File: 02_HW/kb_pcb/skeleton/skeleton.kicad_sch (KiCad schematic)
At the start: 60 parts, among them SW1 SW_Push, SW10 SW_Push, SW11 SW_Push, SW12 SW_Push, SW13 SW_Push, SW14 SW_Push, SW15 SW_Push, SW16 SW_Push, SW17 SW_Push, SW18 SW_Push, SW19 SW_Push, SW2 SW_Push, SW20 SW_Push, SW21 SW_Push, SW22 SW_Push, SW23 SW_Push, SW24 SW_Push, SW25 SW_Push, SW26 SW_Push, SW27 SW_Push, SW28 SW_Push, SW29 SW_Push, SW3 SW_Push, SW30 SW_Push, SW4 SW_Push, SW5 SW_Push, SW6 SW_Push, SW7 SW_Push, SW8 SW_Push, SW9 SW_Push

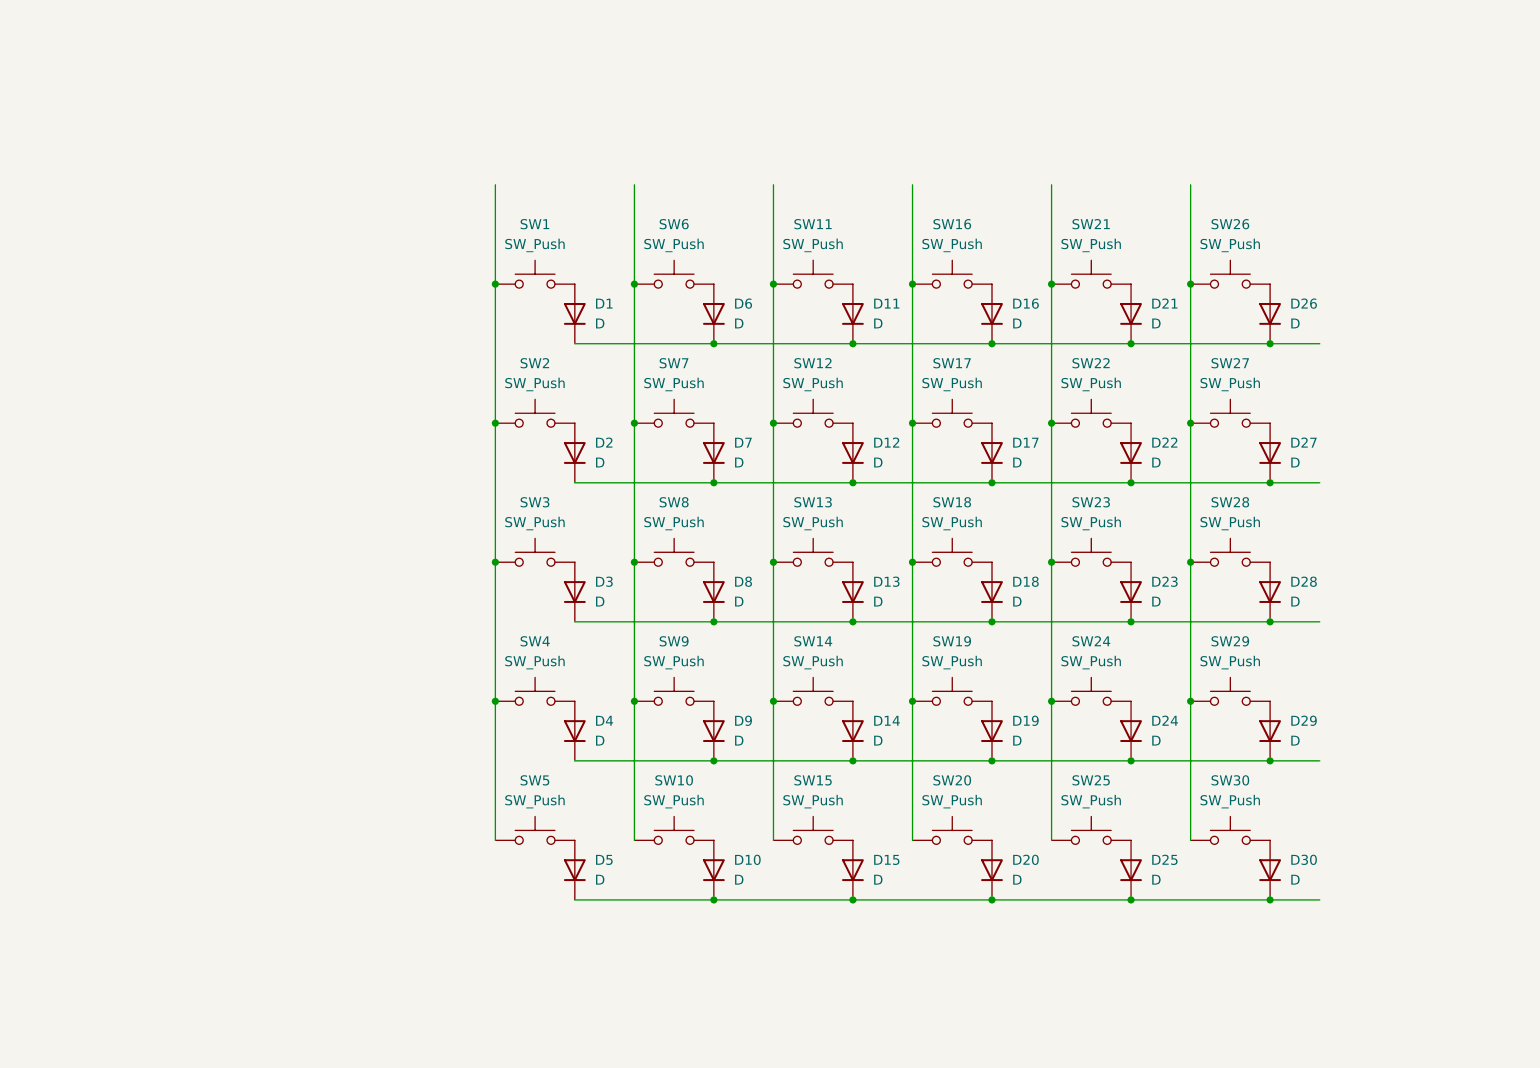
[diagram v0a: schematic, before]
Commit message: Added footprints
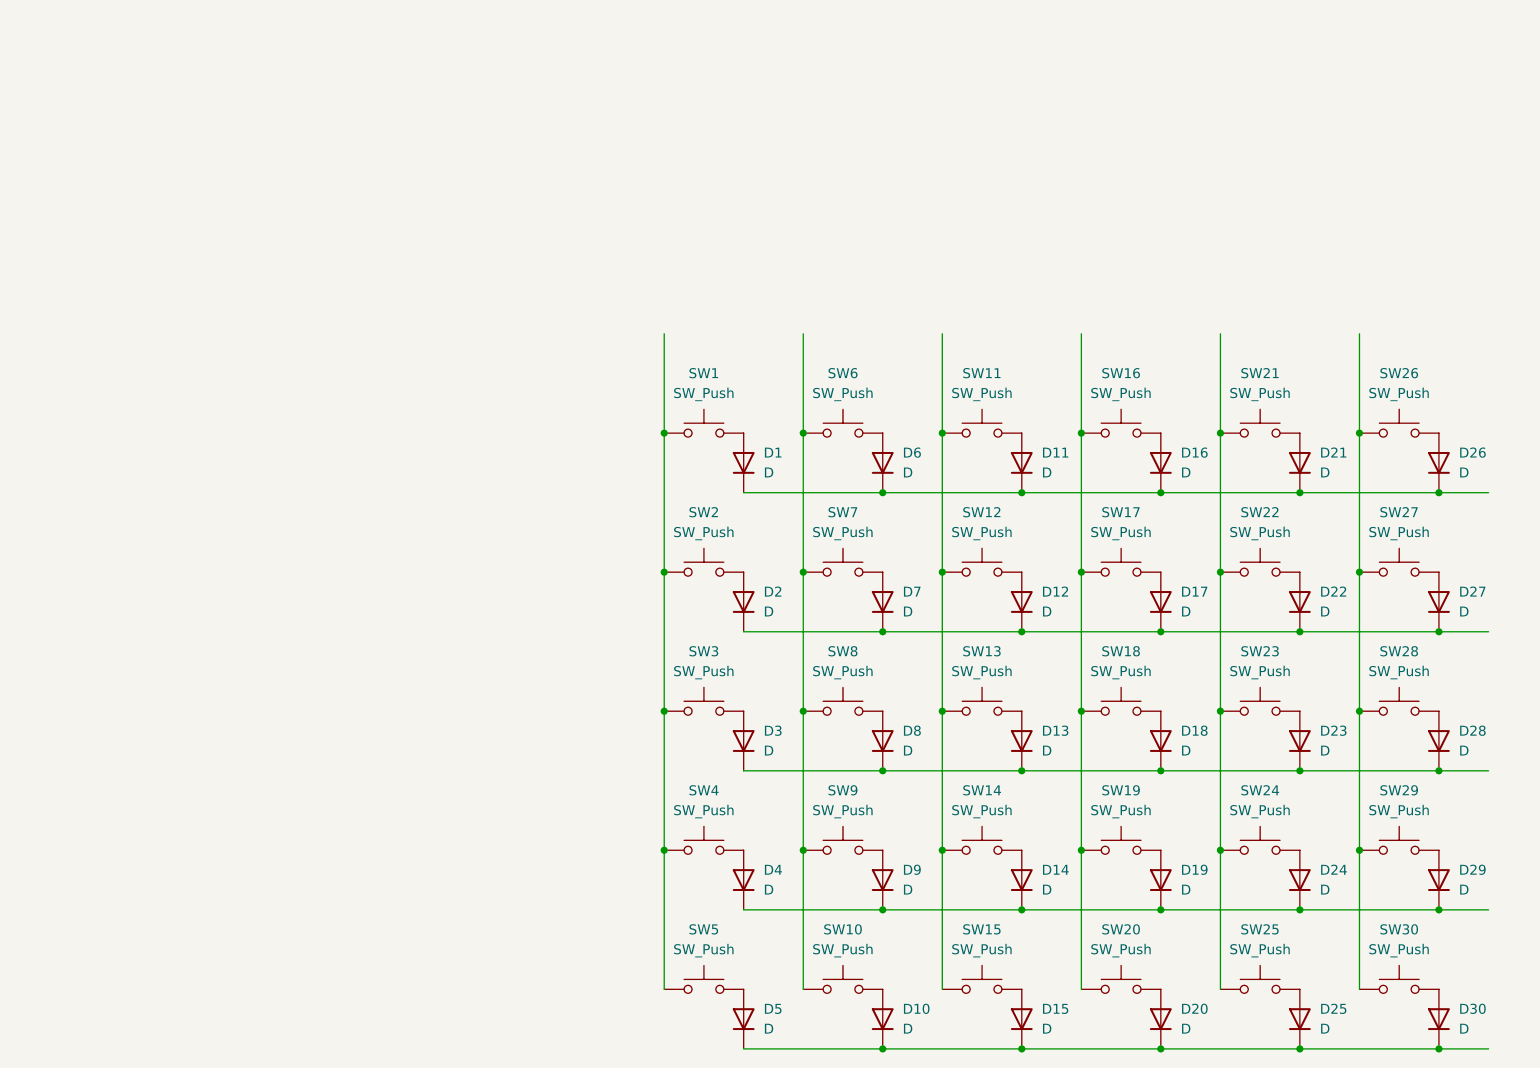
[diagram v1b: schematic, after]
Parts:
- D1, D10, D11, D12, D13, D14, D15, D16, D17, D18, D19, D2, D20, D21, D22, D23, D24, D25, D26, D27, D28, D29, D3, D30, D4, D5, D6, D7, D8, D9: footprint (none) -> Diode_SMD:Nexperia_CFP3_SOD-123W
- SW1, SW10, SW11, SW12, SW13, SW14, SW15, SW16, SW17, SW18, SW19, SW2, SW20, SW21, SW22, SW23, SW24, SW25, SW26, SW27, SW28, SW29, SW3, SW30, SW4, SW5, SW6, SW7, SW8, SW9: footprint (none) -> PCM_Switch_Keyboard_Cherry_MX:SW_Cherry_MX_PCB_1.25u
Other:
- moved on the sheet: D1, D10, D11, D12, D13, D14, D15, D16, D17, D18, D19, D2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

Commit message: Added header pins and diodes. Updated PCB from schematic
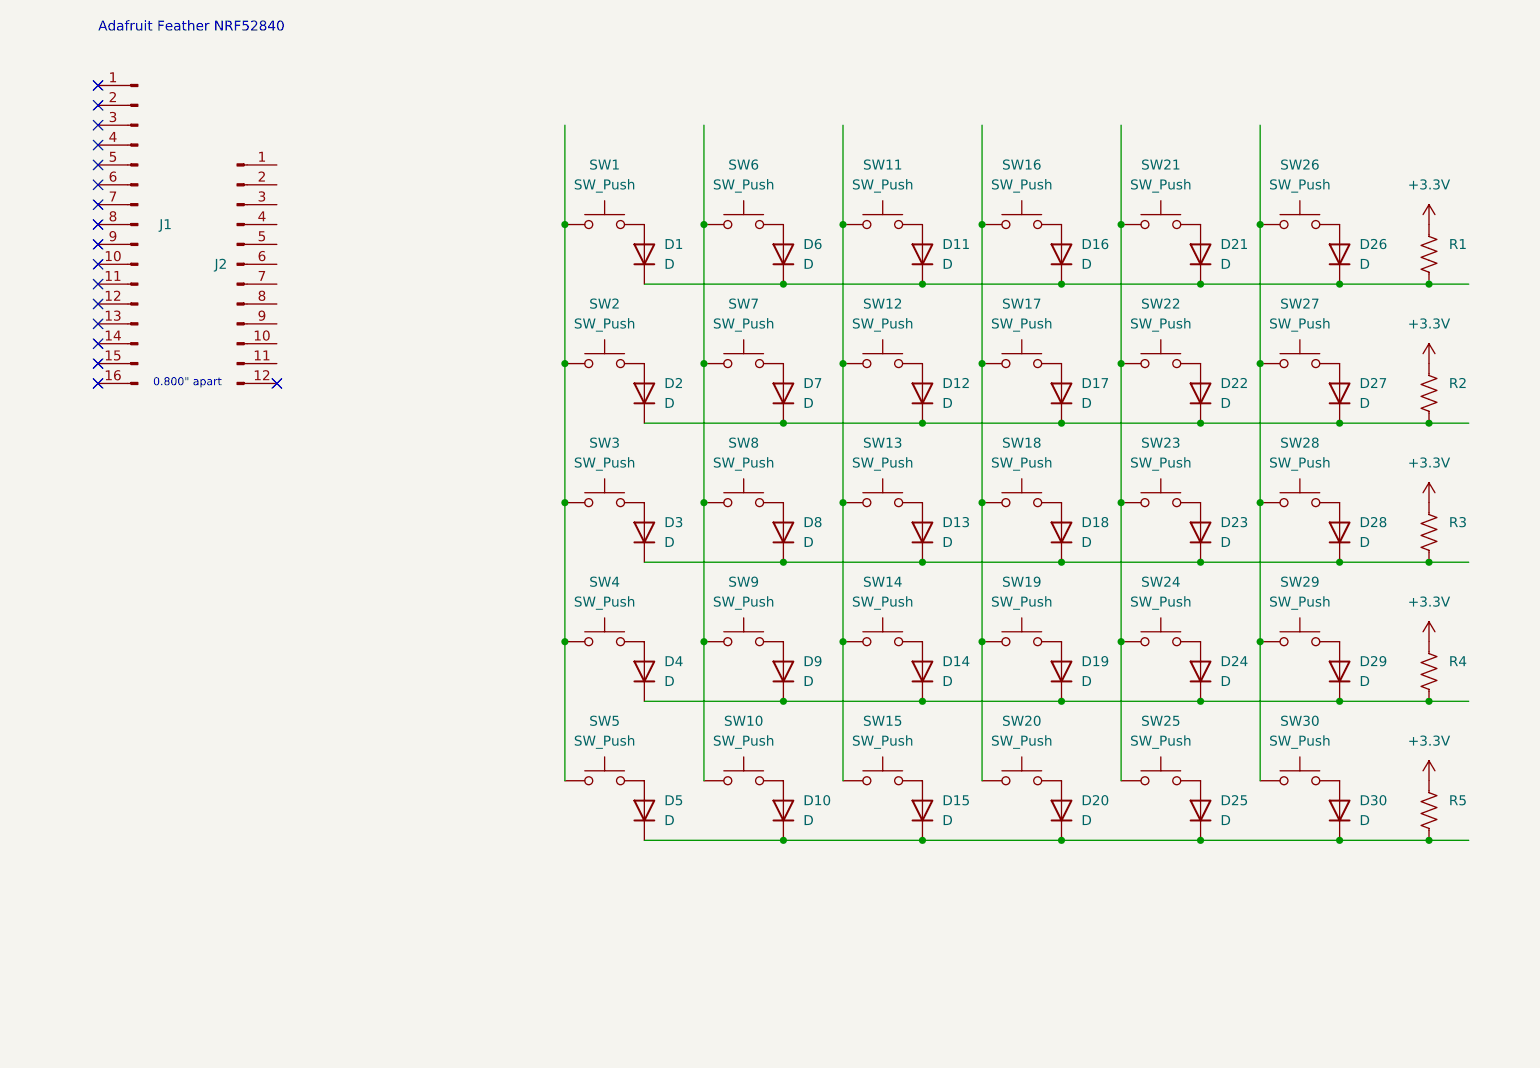
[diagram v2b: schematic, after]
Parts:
- added J1: Adafruit_Feather_16_pin, Connector_PinSocket_2.54mm:PinSocket_1x16_P2.54mm_Vertical, symbol Connector:Conn_01x16_Pin
- added J2: Adafruit_feather_12_pin, Connector_PinHeader_2.54mm:PinHeader_1x12_P2.54mm_Vertical, symbol Connector:Conn_01x12_Pin
- added R1, R2, R3, R4, R5: R_US, Button_Switch_Keyboard:SW_Cherry_MX_1.00u_PCB, symbol Device:R_US
- SW1, SW10, SW11, SW12, SW13, SW14, SW15, SW16, SW17, SW18, SW19, SW2, SW20, SW21, SW22, SW23, SW24, SW25, SW26, SW27, SW28, SW29, SW3, SW30, SW4, SW5, SW6, SW7, SW8, SW9: footprint PCM_Switch_Keyboard_Cherry_MX:SW_Cherry_MX_PCB_1.25u -> Button_Switch_Keyboard:SW_Cherry_MX_1.00u_PCB
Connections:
- net at D14.1 (K), D19.1 (K), D24.1 (K)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: now also R4.2
- net at D13.1 (K), D18.1 (K), D23.1 (K)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: now also R3.2
- net at D1.1 (K), D11.1 (K), D16.1 (K)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: now also R1.2
- net at D10.1 (K), D15.1 (K), D20.1 (K)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: now also R5.2
- net at D12.1 (K), D17.1 (K), D2.1 (K)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: now also R2.2
- new net +3.3V: R1.1, R2.1, R3.1, R4.1, R5.1
- no-connect marks 0 -> 17
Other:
- note added: "0.800" apart"
- note added: "Adafruit Feather NRF52840"
- moved on the sheet: D1, D10, D11, D12, D13, D14, D15, D16, D17, D18, D19, D2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

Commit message: Organized key layout
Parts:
- R1, R2, R3, R4, R5: footprint Button_Switch_Keyboard:SW_Cherry_MX_1.00u_PCB -> Resistor_SMD:R_0603_1608Metric
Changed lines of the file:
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@@
 			)
 		)
-		(property "Footprint" "Button_Switch_Keyboard:SW_Cherry_MX_1.00u_PCB"
+		(property "Footprint" "Resistor_SMD:R_0603_1608Metric"
 			(at 195.326 90.424 90)
 			(effects
@@
 			)
 		)
-		(property "Footprint" "Button_Switch_Keyboard:SW_Cherry_MX_1.00u_PCB"
+		(property "Footprint" "Resistor_SMD:R_0603_1608Metric"
 			(at 195.326 125.984 90)
 			(effects
@@
 			)
 		)
-		(property "Footprint" "Button_Switch_Keyboard:SW_Cherry_MX_1.00u_PCB"
+		(property "Footprint" "Resistor_SMD:R_0603_1608Metric"
 			(at 195.326 54.864 90)
 			(effects
@@
 			)
 		)
-		(property "Footprint" "Button_Switch_Keyboard:SW_Cherry_MX_1.00u_PCB"
+		(property "Footprint" "Resistor_SMD:R_0603_1608Metric"
 			(at 195.326 108.204 90)
 			(effects
@@
 			)
 		)
-		(property "Footprint" "Button_Switch_Keyboard:SW_Cherry_MX_1.00u_PCB"
+		(property "Footprint" "Resistor_SMD:R_0603_1608Metric"
 			(at 195.326 72.644 90)
 			(effects

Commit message: Positioned key switch columns. Began fixing net labels
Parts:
- removed D5: D, Diode_SMD:Nexperia_CFP3_SOD-123W, symbol Device:D
- removed SW5: SW_Push, Button_Switch_Keyboard:SW_Cherry_MX_1.00u_PCB, symbol Switch:SW_Push
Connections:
- net Row_3: now reaches D14.1 (K), D19.1 (K), D24.1 (K), D29.1 (K), D4.1 (K), D9.1 (K), R4.2
- net Row_2: now reaches D13.1 (K), D18.1 (K), D23.1 (K), D28.1 (K), D3.1 (K), D8.1 (K), R3.2
- net Row_0: now reaches D1.1 (K), D11.1 (K), D16.1 (K), D21.1 (K), D26.1 (K), D6.1 (K), R1.2
- net Row_4: now reaches D10.1 (K), D15.1 (K), D20.1 (K), D25.1 (K), D30.1 (K), R5.2
- net Row_1: now reaches D12.1 (K), D17.1 (K), D2.1 (K), D22.1 (K), D27.1 (K), D7.1 (K), R2.2

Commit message: moved thumb pad, fixed net labels,added design rules
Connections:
- net Row_0: now also J2.12 (Pin_12)
- net Row_1: now also J2.11 (Pin_11)
- net Row_2: now also J2.10 (Pin_10)
- net Row_3: now also J2.9 (Pin_9)
- net Row_4: now also J2.8 (Pin_8)
- net Col_0: now reaches SW1.1, SW2.1, SW3.1, SW4.1
- net Col_0: now also J1.6 (Pin_6)
- net Col_4: now reaches SW21.1, SW22.1, SW23.1, SW24.1, SW25.1
- net Col_4: now also J1.10 (Pin_10)
- net Col_5: now reaches J1.11 (Pin_11)
- net Col_5: now also SW26.1, SW27.1, SW28.1, SW29.1, SW30.1
- net Col_1: now reaches J1.7 (Pin_7)
- net Col_1: now also SW10.1, SW6.1, SW7.1, SW8.1, SW9.1
- net Col_2: now reaches J1.8 (Pin_8)
- net Col_2: now also SW11.1, SW12.1, SW13.1, SW14.1, SW15.1
- net Col_3: now reaches J1.9 (Pin_9)
- net Col_3: now also SW16.1, SW17.1, SW18.1, SW19.1, SW20.1
